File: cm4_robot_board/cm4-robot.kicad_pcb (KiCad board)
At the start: 4 copper layers, 118 x 118 mm, 163 parts, among them J1 1747981-1, J10 Conn_01x04, J11 Conn_01x03, J12 Conn_01x04, J13 RJ45, J14 RJ45, J15 RJ45, J16 RJ45, J17 Conn_01x04, J18 Conn_01x04, J19 Conn_01x04, J2 HR913550A, J20 Conn_01x04, J21 Conn_01x03, J22 Conn_01x04, J23 Conn_01x01, J24 Conn_01x01, J3 USB_C_Receptacle_USB2.0, J4 Conn_01x04, J5 Conn_01x04, J6 Conn_01x04, J7 USB_A, J8 HIGHCURRENTPAD2, J9 HIGHCURRENTPAD2, Q1 Q_PMOS_GSD, Q2 Q_NMOS_GSD, Q3 Q_NMOS_GSD, Q4 Q_NMOS_GSD, Q5 Q_NMOS_GSD, SW1 B3U-1000P, SW2 SW_SPDT, SW3 SW_SPDT, U1 SN74LVC1G07QDCKTQ1, U10 isolator, U11 isolator, U12 TPS61040DBVR, U13 SC16IS752, U14 SC16IS752, U15 SN74LVC1G07QDCKTQ1, U16 CC56-12SEKWA, U17 ET6226M, U18 SN74LVC1G07QDCKTQ1, U19 SN74LVC1G07QDCKTQ1, U2 SN74LVC1G07QDCKTQ1, U3 LM2576HVS-5, U4 TPD4E1U06DCKR, U5 ISL54222AIUZ, U6 LTC4412xS6, U7 SN74HC08N, U8 MCP2515-xSO, U9 MCP2515-xSO, Y1 Crystal_GND24, Y2 Crystal_GND24, Y3 Crystal_GND24, Y4 Crystal_GND24

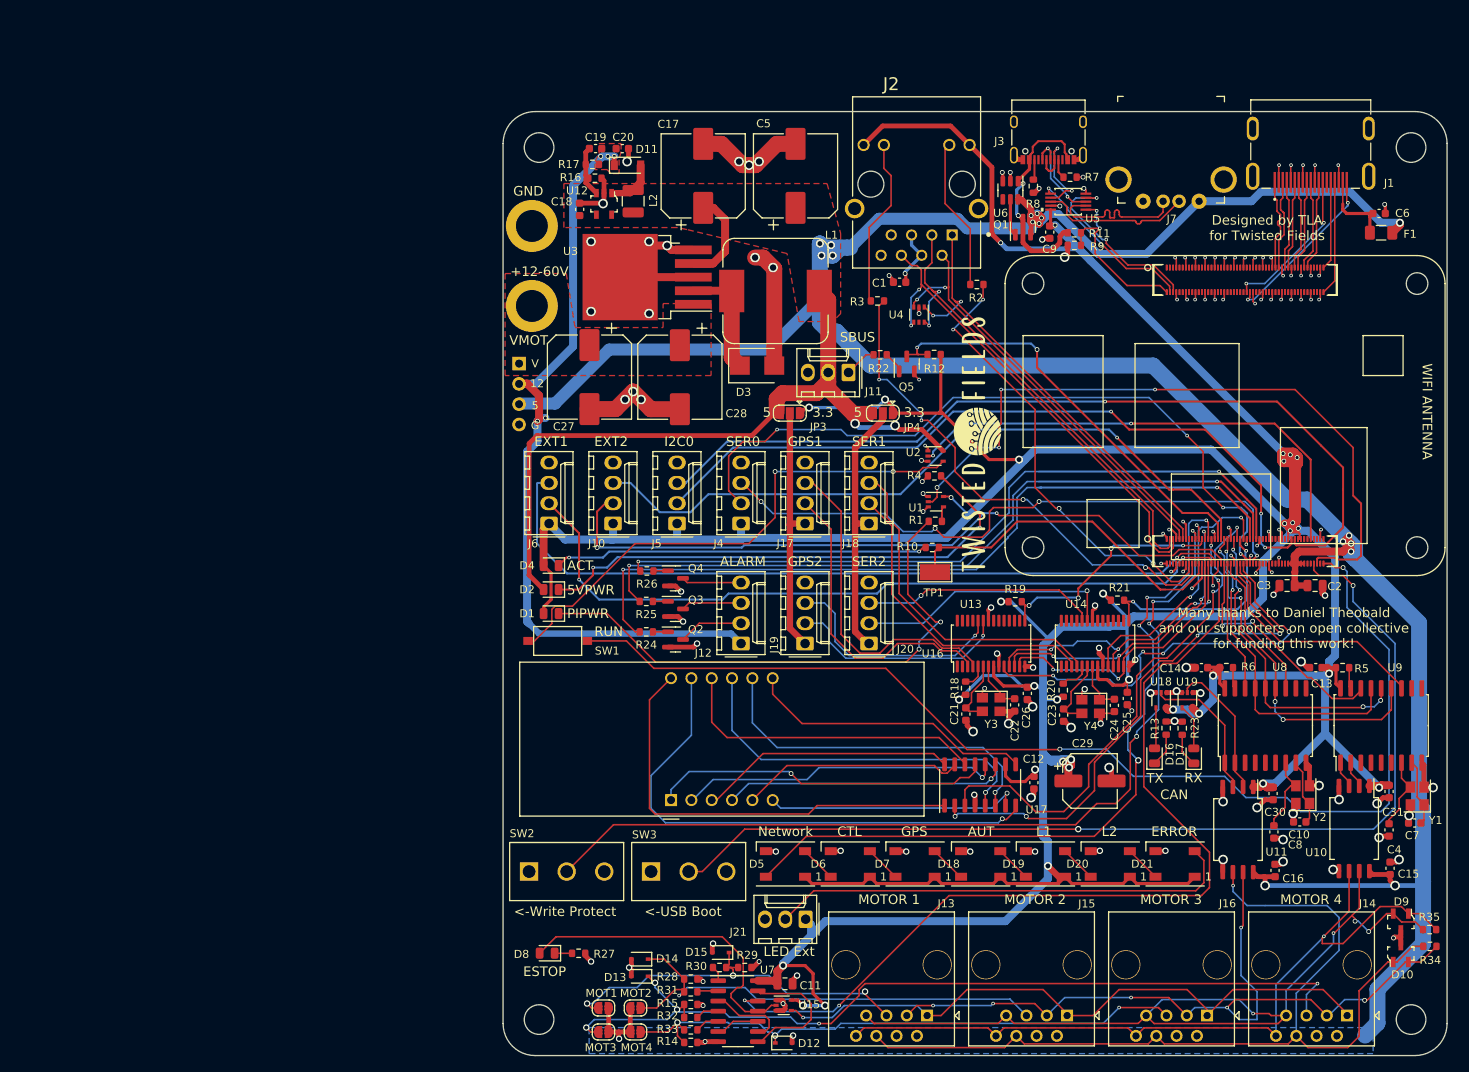
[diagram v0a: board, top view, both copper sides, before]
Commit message: Update latest files for CM4 robot board. Ordered this version.
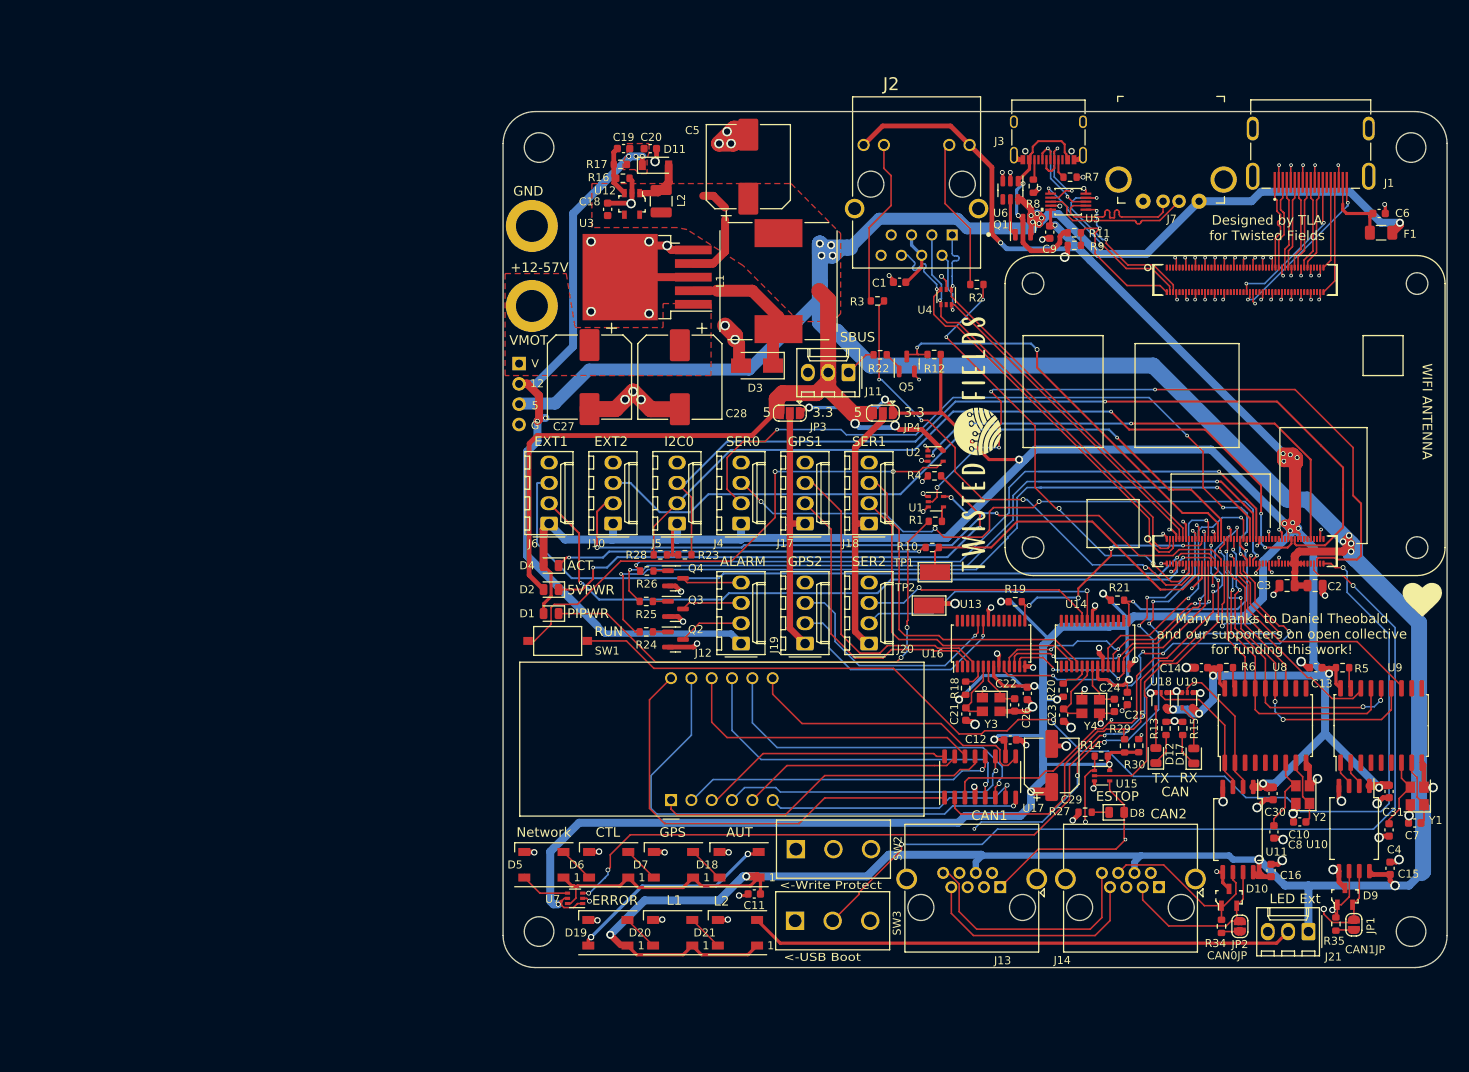
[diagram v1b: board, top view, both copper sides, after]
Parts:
- removed C17: 1000uF, Capacitor_SMD:CP_Elec_10x10
- removed D13, D14, D15: D_TVS, Diode_SMD:D_SOD-323
- removed D16: LED_GREEN, LED_SMD:LED_0805_2012Metric
- removed J15, J16: RJ45, Connector_RJ:RJ45_OST_PJ012-8P8CX_Vertical
- removed JP5, JP6, JP7, JP8: SolderJumper_2_Open, Jumper:SolderJumper-2_P1.3mm_Open_RoundedPad1.0x1.5mm
- removed R31, R32, R33: 1k, Resistor_SMD:R_0603_1608Metric
- added JP1: SolderJumper_2_Open, Jumper:SolderJumper-2_P1.3mm_Open_RoundedPad1.0x1.5mm, F.Cu at (146.3, 141.7)
- added JP2: SolderJumper_2_Open, Jumper:SolderJumper-2_P1.3mm_Open_RoundedPad1.0x1.5mm, F.Cu at (132.1, 141.8)
- added TP2: TestPoint, TestPoint:TestPoint_Keystone_5019_Minature, F.Cu at (93.2, 101.8)
- C10, C4, C7, C8: value 10p -> 18p
- C11: value 10uF -> 0.1uF; footprint Capacitor_SMD:C_0805_2012Metric -> Capacitor_SMD:C_0603_1608Metric
- C18: value 10uF -> 4.7uF
- C19: value 4.7pF -> 2.7pF
- C20: value 4.7uF -> 1uF
- C21, C22, C23, C24: value 12pF -> 22p
- D12: value D_TVS -> LED_GREEN; footprint Diode_SMD:D_SOD-323 -> LED_SMD:LED_0805_2012Metric
- D3: footprint Diode_SMD:D_SMB -> Diode_SMD:D_SMA
- J13, J14: footprint Connector_RJ:RJ45_OST_PJ012-8P8CX_Vertical -> parts:RJ45_R-RJ45R08P-B000
- L1: footprint parts:MWSA1206S-680MT -> parts:L_15mmx15mm
- R13: value 220R -> 27R
- R15: value 10k -> 56R
- R23: value 220R -> 10k
- R30: value 1k -> 10k
- U7: value SN74HC08N -> TXS0101DCKR; footprint Package_SO:SOIC-14_3.9x8.7mm_P1.27mm -> Package_TO_SOT_SMD:SOT-363_SC-70-6
- moved D8 73.3 mm to (116.7, 127.6), turned to 0 degrees
- moved R15 70.5 mm to (125.0, 117.1), turned to -90 degrees
- moved R23 65.8 mm to (62.7, 95.4), turned to 0 degrees
- moved R27 65.7 mm to (112.8, 127.6), turned to 180 degrees
- moved J21 62.9 mm to (140.7, 142.5)
- moved R14 62.6 mm to (114.8, 120.6), turned to 180 degrees
- moved R30 59.3 mm to (119.5, 119.3), turned to 90 degrees
- moved D12 58.8 mm to (121.6, 120.5), turned to 90 degrees
- moved D19 55.4 mm to (53.1, 142.7)
- moved D20 55.4 mm to (61.2, 142.7)
- moved D21 55.4 mm to (69.3, 142.7)
- moved R29 55.0 mm to (117.7, 119.3), turned to 90 degrees
- moved R28 53.2 mm to (59.6, 95.4), turned to 180 degrees
- moved U15 49.1 mm to (114.9, 123.0)
- moved SW2 33.5 mm to (76.6, 132.2)
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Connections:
- C11 pad 1: +3V3 -> +5V
- D12 pad 1: E4B -> Net-(D12-Pad1)
- D12 pad 2: GND -> Net-(D12-Pad2)
- D18 pad 1: +3V3 -> +5V
- D19 pad 1: +3V3 -> +5V
- D20 pad 1: +3V3 -> +5V
- D21 pad 1: +3V3 -> +5V
- D5 pad 1: +3V3 -> +5V
- D5 pad 4: WS2812 -> Net-(D5-Pad4)
- D6 pad 1: +3V3 -> +5V
- D7 pad 1: +3V3 -> +5V
- D8 pad 2: Net-(D8-Pad2) -> ESTOP_OUT
- J13 pad 5: E1B -> ESTOP_SINK
- J14 pad 5: E3B -> ESTOP_SINK
- J21 pad 1: +3V3 -> +5V
- J24 pad 1: unconnected-(J24-Pad1) -> GND
- R13 pad 1: Net-(D16-Pad1) -> GND
- R13 pad 2: GND -> Net-(D12-Pad1)
- R14 pad 1: E4B -> +3V3
- R14 pad 2: GND -> ESTOP_SINK
- R15 pad 1: E3B -> GND
- R15 pad 2: GND -> Net-(D17-Pad1)
- R23 pad 1: Net-(D17-Pad1) -> +3V3
- R23 pad 2: GND -> SDA0_GPIO44
- R28 pad 1: E2B -> +3V3
- R28 pad 2: GND -> SCL0_GPIO45
- R29 pad 1: E1B -> +3V3
- R29 pad 2: GND -> SCL6
- R30 pad 1: Net-(R30-Pad1) -> +3V3
- R30 pad 2: E1B -> SDA6
- R34 pad 1: CANH0 -> CANL0
- R34 pad 2: CANL0 -> Net-(JP2-Pad2)
- R35 pad 1: CANH1 -> CANL1
- R35 pad 2: CANL1 -> Net-(JP1-Pad2)
- U15 pad 1: GND -> ESTOP_SINK
- U15 pad 2: Net-(D8-Pad2) -> ESTOP
- U18 pad 4: Net-(D16-Pad2) -> Net-(D12-Pad2)
- U4 pad 3: TRD0_N -> TRD1_N
- U4 pad 4: TRD1_N -> TRD1_P
- U4 pad 6: TRD1_P -> TRD0_N
- U7 pad 1: Net-(R30-Pad1) -> +3V3
- U7 pad 2: Net-(R31-Pad1) -> GND
- U7 pad 3: E12B -> WS2812
- U7 pad 4: Net-(R32-Pad1) -> Net-(D5-Pad4)
- U7 pad 5: Net-(R33-Pad1) -> +3V3
- U7 pad 6: E34B -> +5V
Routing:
- net +5V: track 471.7 -> 594.1 mm, vias 19 -> 20
- net E3B: track 110.3 -> 0.00 mm, vias 5 -> 0
- net ESTOP: track 119.1 -> 40.4 mm, vias 4 -> 2
- net E4B: track 73.3 -> 0.00 mm, vias 3 -> 0
- net CANL0: track 114.5 -> 44.0 mm, vias 1 -> 0
- net E2B: track 59.8 -> 0.00 mm, vias 1 -> 0
- net CANH0: track 98.4 -> 46.5 mm, vias 6 -> 0
- net E1B: track 48.3 -> 0.00 mm, vias 3 -> 0
- net ESTOP_OUT: track 79.8 -> 34.2 mm
- net Net-(D8-Pad2): track 40.0 -> 0.00 mm
- net +3V3: track 632.3 -> 592.7 mm, vias 34 -> 30
- net ESTOP_SINK: track 0.00 -> 39.0 mm, vias 0 -> 1
- net EEPROM_nWP: track 113.8 -> 77.3 mm, vias 4 -> 6
- net CANH1: track 107.7 -> 73.3 mm, vias 4 -> 1
- net CANL1: track 97.7 -> 75.6 mm
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- removed copper zone on B.Cu, net +5V
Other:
- board size 118 x 118 mm -> 118 x 107 mm
- board text added: "+12-57V"
- board text added: "CAN0JP"
- board text added: "CAN1"
- board text added: "CAN1JP"
- board text added: "CAN2"
- board text removed: "+12-60V"
- board text removed: "MOT1"
- board text removed: "MOT2"
- board text removed: "MOT3"
- board text removed: "MOT4"
- board text removed: "MOTOR 1"
- board text removed: "MOTOR 2"
- board text removed: "MOTOR 3"
- board text removed: "MOTOR 4"

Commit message: Rev 2 Supercap PCB, updates to Motherboard in progress
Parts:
- removed R14: 10k, Resistor_SMD:R_0603_1608Metric
- removed TP2: TestPoint, TestPoint:TestPoint_Keystone_5019_Minature
- added C17: 10u, Capacitor_SMD:C_0805_2012Metric, F.Cu at (-8.84, 88.2)
- added C32: 10u, Capacitor_SMD:C_0805_2012Metric, F.Cu at (-8.84, 91.2)
- added C33: 47uF 16V, Capacitor_SMD:C_1210_3225Metric, F.Cu at (-18.8, 88.8)
- added C34: 22pF, Capacitor_SMD:C_0603_1608Metric, F.Cu at (-4.61, 87.9)
- added C35: 22uF 10v, Capacitor_SMD:C_0805_2012Metric, F.Cu at (-8.84, 94.2)
- added C36: 22uF 6.3v, Capacitor_SMD:C_0603_1608Metric, F.Cu at (-4.61, 90.4)
- added C37: 22uF 6.3v, Capacitor_SMD:C_0603_1608Metric, F.Cu at (-4.61, 92.9)
- added C38: 47uF 16V, Capacitor_SMD:C_1210_3225Metric, F.Cu at (-18.8, 93.0)
- added C39: 0.1uF, Capacitor_SMD:C_0805_2012Metric, F.Cu at (69.5, 38.3)
- added C42: 22nF 100v, Capacitor_SMD:C_0603_1608Metric, F.Cu at (99.6, 52.4)
- added C43: 1nF 2kV, Capacitor_SMD:C_1206_3216Metric, F.Cu at (106.9, 54.9)
- added C44: 22nF 100v, Capacitor_SMD:C_0603_1608Metric, F.Cu at (99.6, 54.0)
- added C45: 22nF 100v, Capacitor_SMD:C_0603_1608Metric, F.Cu at (99.6, 55.7)
- added C46: 22nF 100v, Capacitor_SMD:C_0603_1608Metric, F.Cu at (99.6, 57.4)
- added C47: 0.1uF, Capacitor_SMD:C_0603_1608Metric, F.Cu at (81.2, 51.7)
- added D13: ABS2, Diode_SMD:Diode_Bridge_Diotec_ABS, F.Cu at (76.7, 36.2)
- added D14: LED_GREEN, LED_SMD:LED_0805_2012Metric, F.Cu at (100.2, 48.3)
- added D15: SMAJ60A, Diode_SMD:D_SMA, F.Cu at (70.4, 32.4)
- added D16: D, Diode_SMD:D_SMA, F.Cu at (56.5, 40.7)
- added D22: ABS2, Diode_SMD:Diode_Bridge_Diotec_ABS, F.Cu at (76.8, 44.9)
- added D23: LED_YELLOW, LED_SMD:LED_0805_2012Metric, F.Cu at (100.2, 50.4)
- added D24: 28V / 500mW, Diode_SMD:D_SOD-123, F.Cu at (64.2, 33.6)
- added D25: 15V / 200mW, Diode_SMD:D_SOD-323, F.Cu at (65.3, 38.2)
- added J15: Conn_02x04_Odd_Even, Connector_PinHeader_2.54mm:PinHeader_2x04_P2.54mm_Vertical, F.Cu at (48.5, 48.2)
- added J25: RJ45, parts:RJ45_R-RJ45R08P-B000, F.Cu at (86.1, 37.9)
- added JP5: SolderJumper_2_Open, Jumper:SolderJumper-2_P1.3mm_Open_RoundedPad1.0x1.5mm, F.Cu at (-8.88, 97.5)
- added L3: 10uH, Inductor_SMD:L_Sunlord_SWPA5040S, F.Cu at (-8.43, 81.7)
- added Q6: AO3401A, Package_TO_SOT_SMD:SOT-23, F.Cu at (-13.5, 88.9)
- added Q7: AO3400A, Package_TO_SOT_SMD:SOT-23, F.Cu at (-13.5, 93.3)
- added Q8: Si2328DS, Package_TO_SOT_SMD:SOT-23-3, F.Cu at (62.2, 38.3)
- added R31: 82R, Resistor_SMD:R_0603_1608Metric, F.Cu at (52.8, 95.7)
- added R33: 2.2k 1%, Resistor_SMD:R_0603_1608Metric, F.Cu at (-4.61, 95.4)
- added R36: 24.1k/1%, Resistor_SMD:R_0805_2012Metric, F.Cu at (71.9, 38.2)
- added R37: 249k, Resistor_SMD:R_0805_2012Metric, F.Cu at (67.4, 38.3)
- added R40: 51k, Resistor_SMD:R_0805_2012Metric, F.Cu at (60.7, 34.5)
- added R41: 75R 100v, Resistor_SMD:R_0603_1608Metric, F.Cu at (102.8, 52.4)
- added R42: 75R 100v, Resistor_SMD:R_0603_1608Metric, F.Cu at (102.8, 54.0)
- added R43: 75R 100v, Resistor_SMD:R_0603_1608Metric, F.Cu at (102.8, 55.7)
- added R44: 75R 100v, Resistor_SMD:R_0603_1608Metric, F.Cu at (102.8, 57.4)
- added SW4: SW_SPDT, parts:CS12ANW03, F.Cu at (121.1, 52.7)
- added TP3: TestPoint, TestPoint:TestPoint_Loop_D2.60mm_Drill1.6mm_Beaded, F.Cu at (89.6, 60.6)
- added TR1: G2401CG, Transformer_SMD:Transformer_Ethernet_YDS_30F-51NL_SO-24_7.1x15.1mm, F.Cu at (90.0, 52.4)
- added U20: NCP1117-3.3_SOT223, Package_TO_SOT_SMD:SOT-223-3_TabPin2, F.Cu at (-16.7, 82.5)
- added U22: MT2492, Package_TO_SOT_SMD:SOT-23-6, F.Cu at (-19.0, 97.4)
- added U23: TPD4E1U06DCKR, Package_TO_SOT_SMD:SOT-363_SC-70-6, F.Cu at (93.9, 63.5)
- C1: value 0.1uF -> 47uF 63V solid; footprint Capacitor_SMD:C_0603_1608Metric -> Capacitor_THT:CP_Radial_D8.0mm_P3.50mm
- C19: value 2.7pF -> 22pF
- D18, D19, D20, D21, D5, D6, D7: footprint LED_SMD:LED_WS2812B_PLCC4_5.0x5.0mm_P3.2mm -> parts:LED_WS2812B_PLCC4_5.0x5.0mm_P3.2mm
- D3: footprint Diode_SMD:D_SMA -> Diode_SMD:D_SMC
- J13: value RJ45 -> CAN Interface; footprint parts:RJ45_R-RJ45R08P-B000 -> parts:M12A-08PFFR
- J14: value RJ45 -> Conn_01x03; footprint parts:RJ45_R-RJ45R08P-B000 -> Connector_Molex:Molex_KK-254_AE-6410-03A_1x03_P2.54mm_Vertical
- J2: value HR913550A -> CAN Interface; footprint parts:HANRUN_HR911105A -> parts:M12A-08PFFR
- R4: value 220R -> 2.2k 1%
- Y1, Y2: value Crystal_GND24 -> 16MHz
- Y3, Y4: value Crystal_GND24 -> 14.7456MHz
- moved J2 99.4 mm to (99.0, 148.2)
- moved J14 89.6 mm to (149.7, 51.8), turned to 0 degrees
- moved C1 42.3 mm to (56.9, 34.5), turned to 180 degrees
- moved R4 40.7 mm to (114.9, 120.4), turned to 0 degrees
- moved J13 19.3 mm to (117.7, 148.3), turned to 0 degrees
- moved C6 10.0 mm to (149.5, 42.7)
- moved C9 10.0 mm to (108.3, 45.1)
- moved F1 10.0 mm to (149.8, 45.1)
- moved H1 10.0 mm to (44.5, 34.5)
- moved H3 10.0 mm to (153.5, 34.5)
- moved J1 10.0 mm to (141.0, 38.1)
- moved J3 10.0 mm to (108.2, 32.3)
- moved J7 10.0 mm to (123.5, 38.5)
- moved Q1 10.0 mm to (105.0, 44.5)
- moved R11 10.0 mm to (111.4, 45.1)
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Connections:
- C1 pad 1: GND -> VOUTP
- C1 pad 2: Net-(C1-Pad2) -> GND
- D1 pad 2: +3V3 -> LED_PWR
- D10 pad 1: CANL0 -> /CAN0_N
- D10 pad 2: CANH0 -> /CAN0_P
- D12 pad 1: Net-(D12-Pad1) -> Net-(D12-K)
- D12 pad 2: Net-(D12-Pad2) -> Net-(D12-A)
- D17 pad 1: Net-(D17-Pad1) -> Net-(D17-K)
- D17 pad 2: Net-(D17-Pad2) -> Net-(D17-A)
- D2 pad 1: Net-(D2-Pad1) -> Net-(D2-K)
- D2 pad 2: +5V -> LED_PWR
- D9 pad 1: CANL1 -> /CAN1_N
- D9 pad 2: CANH1 -> /CAN1_P
- J13 pad 1: ESTOP_OUT -> ESTOP_SINK
- J13 pad 2: GND -> /CAN1_P
- J13 pad 3: CANH0 -> /CAN1_N
- J13 pad 4: +5V -> GND
- J13 pad 5: ESTOP_SINK -> /CAN0_P
- J13 pad 6: CANL0 -> ESTOP_OUT
- J13 pad 7: CANH1 -> 5V_switched
- J13 pad 8: CANL1 -> /CAN0_N
- J14 pad 1: ESTOP_OUT -> unconnected-(J14-Pin_1-Pad1)
- J14 pad 2: GND -> /~{5V_EN}
- J14 pad 3: CANH0 -> GND
- J2 pad 1: TRD0_P -> ESTOP_SINK
- J2 pad 2: TRD0_N -> /CAN1_P
- J2 pad 3: TRD1_P -> /CAN1_N
- J2 pad 4: Net-(C1-Pad2) -> GND
- J2 pad 5: Net-(C1-Pad2) -> /CAN0_P
- J2 pad 6: TRD1_N -> ESTOP_OUT
- J2 pad 7: unconnected-(J2-Pad7) -> 5V_switched
- J2 pad 8: GND -> /CAN0_N
- J2 pad 9: +3V3 -> GND
- JP1 pad 1: CANH1 -> /CAN1_P
- JP2 pad 1: CANH0 -> /CAN0_P
- Module1 pad 11: unconnected-(Module1-Pad11) -> TRD2_P
- Module1 pad 3: unconnected-(Module1-Pad3) -> TRD3_P
- Module1 pad 5: unconnected-(Module1-Pad5) -> TRD3_N
- Module1 pad 84: +3V3 -> unconnected-(Module1A-+3.3v_(Output)-Pad84)
- Module1 pad 86: +3V3 -> 3.3V_ENABLE
- Module1 pad 9: unconnected-(Module1-Pad9) -> TRD2_N
- R13 pad 1: GND -> LED_PWR
- R13 pad 2: Net-(D12-Pad1) -> Net-(D12-A)
- R15 pad 1: GND -> LED_PWR
- R15 pad 2: Net-(D17-Pad1) -> Net-(D17-A)
- R2 pad 1: Net-(J2-Pad10) -> Net-(D14-K)
- R3 pad 1: Net-(J2-Pad11) -> Net-(D23-K)
- R34 pad 1: CANL0 -> /CAN0_N
- R35 pad 1: CANL1 -> /CAN1_N
- R4 pad 1: Net-(D2-Pad1) -> ESTOP_SINK
- R4 pad 2: GND -> +3V3
- U10 pad 6: CANL1 -> /CAN1_N
- U10 pad 7: CANH1 -> /CAN1_P
- U11 pad 6: CANL0 -> /CAN0_N
- U11 pad 7: CANH0 -> /CAN0_P
- U18 pad 4: Net-(D12-Pad2) -> Net-(D12-K)
- U19 pad 4: Net-(D17-Pad2) -> Net-(D17-K)
- U3 pad 5: GND -> /~{5V_EN}
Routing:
- net CANL1: track 75.6 -> 0.00 mm, vias 1 -> 0
- net CANH1: track 73.3 -> 0.00 mm, vias 1 -> 0
- net VC2: track 0.00 -> 68.6 mm, vias 0 -> 2
- net Net-(D2-Pad1): track 65.2 -> 0.00 mm, vias 2 -> 0
- net TRD2_P: track 0.00 -> 62.8 mm, vias 0 -> 2
- net TRD2_N: track 0.00 -> 62.7 mm, vias 0 -> 2
- net VC3: track 0.00 -> 62.1 mm, vias 0 -> 2
- net Net-(D21-DOUT): track 68.2 -> 6.15 mm
- net VC4: track 0.00 -> 61.3 mm, vias 0 -> 2
- net VC1: track 0.00 -> 60.7 mm, vias 0 -> 1
- net TRD3_P: track 0.00 -> 59.2 mm, vias 0 -> 2
- net TRD3_N: track 0.00 -> 59.2 mm, vias 0 -> 2
- net VOUTP: track 0.00 -> 53.1 mm
- net CANH0: track 46.5 -> 0.00 mm
- net CANL0: track 44.0 -> 0.00 mm
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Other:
- board size 118 x 107 mm -> 118 x 117 mm
